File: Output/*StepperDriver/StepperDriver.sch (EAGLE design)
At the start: 12 parts

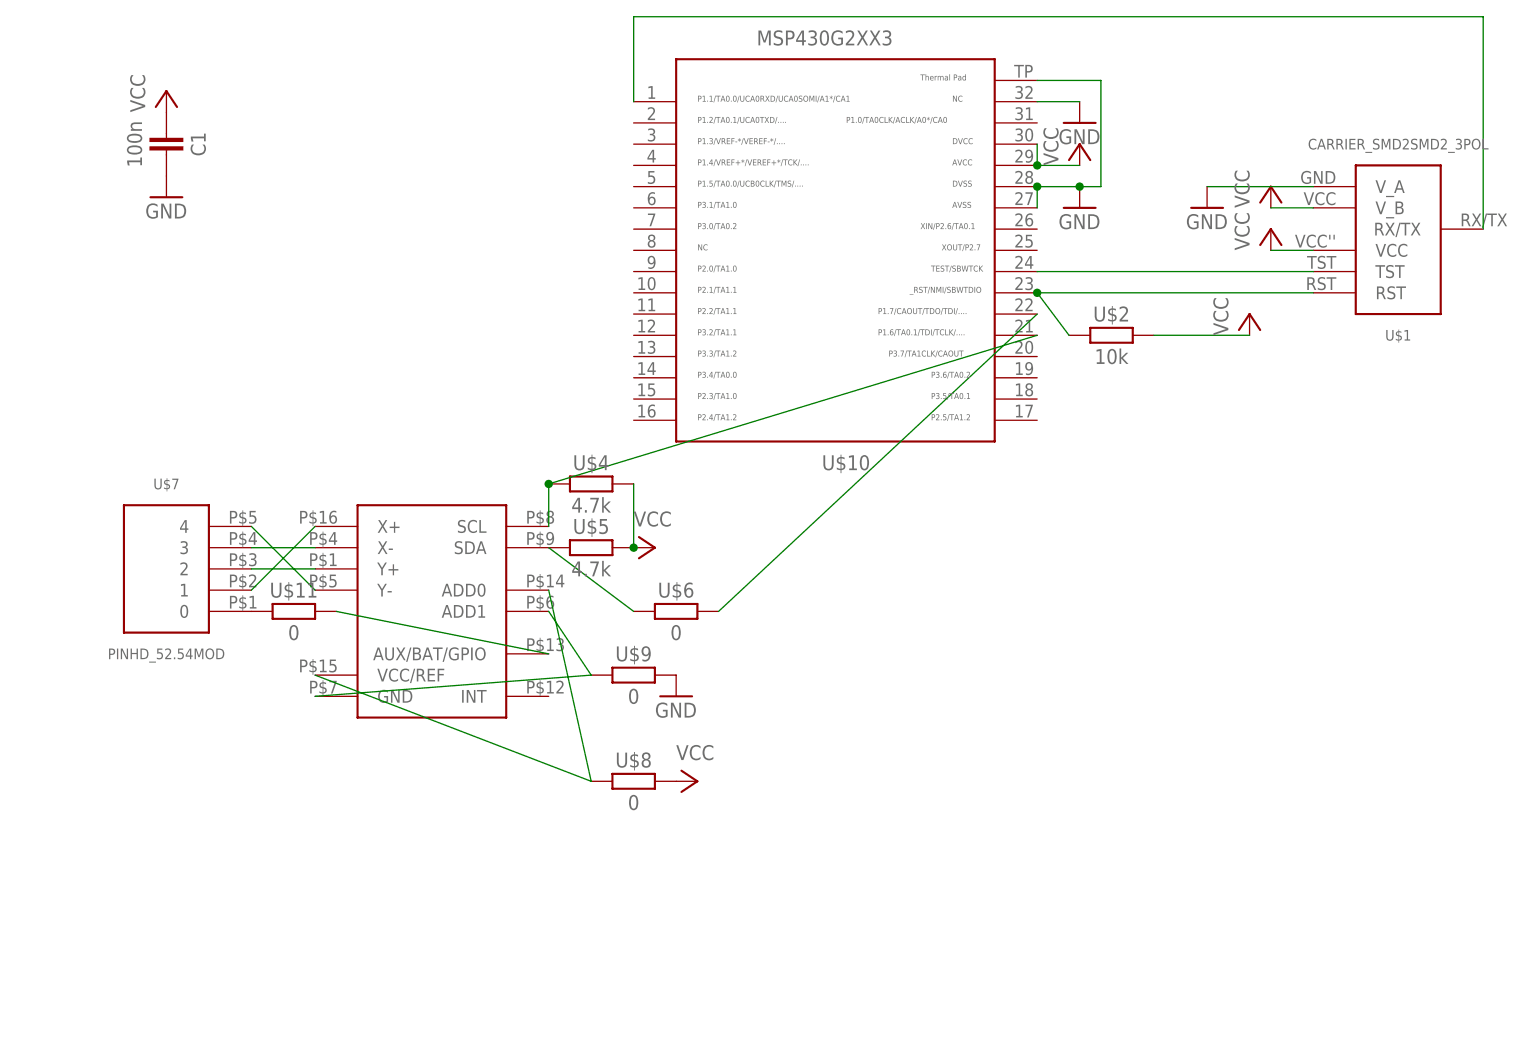
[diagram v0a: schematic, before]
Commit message: Update Pinheader
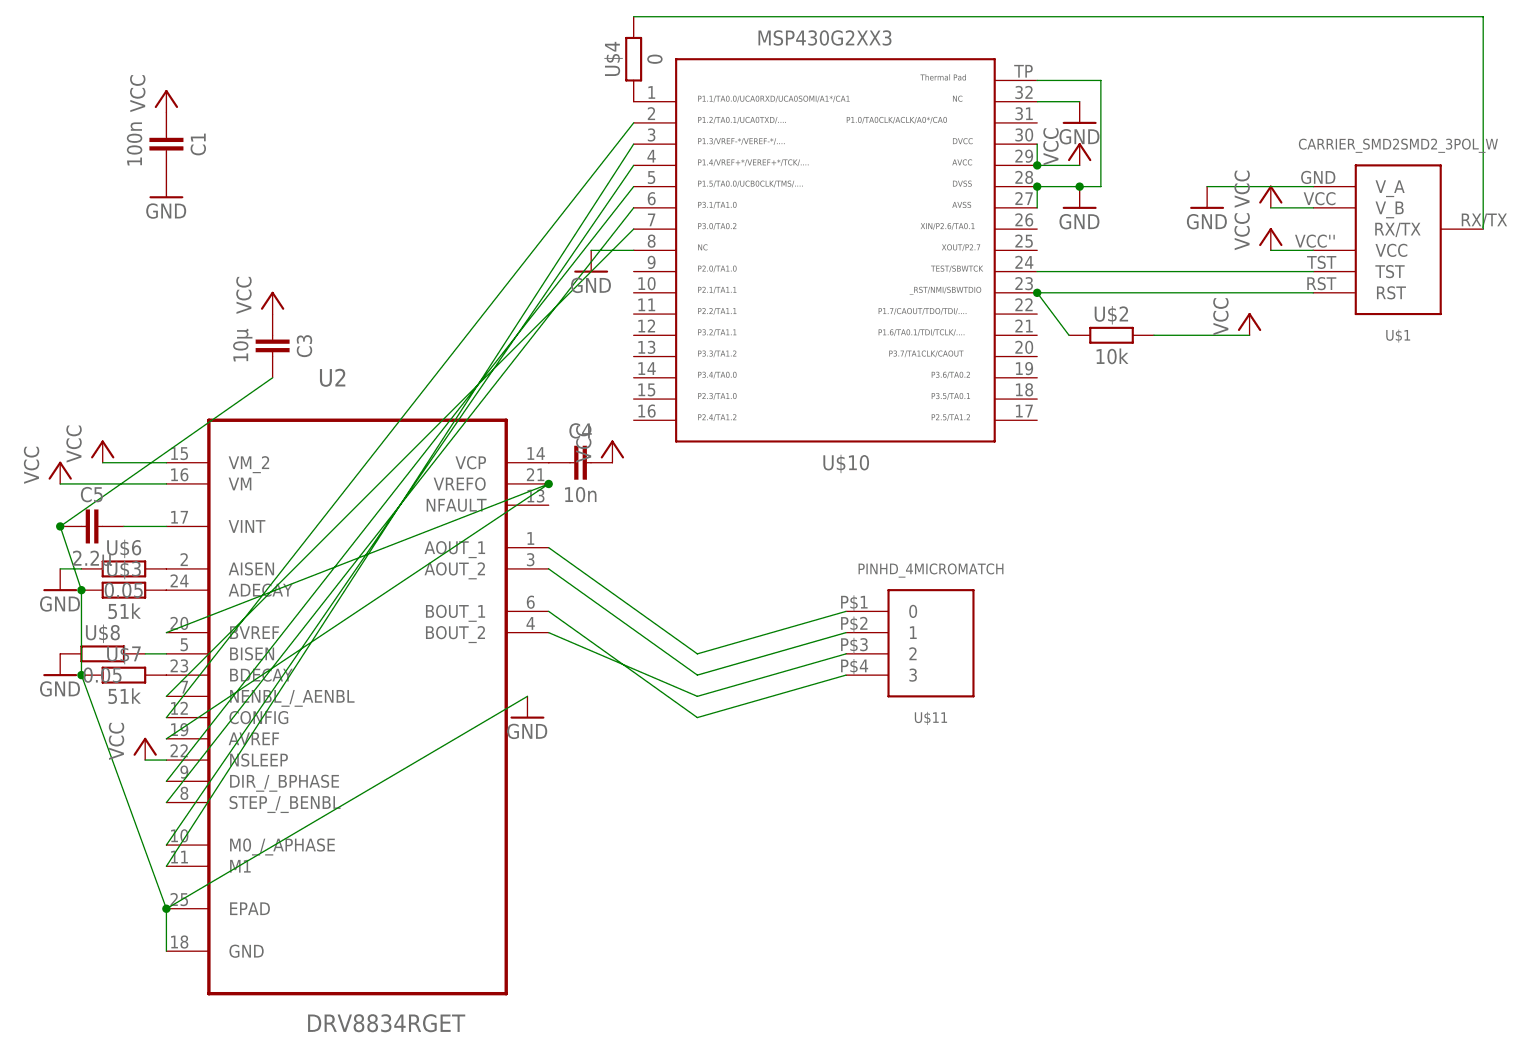
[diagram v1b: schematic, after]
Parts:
- removed U$5: 4.7k, thar:RESISTOR0603
- removed U$9: 0, thar:RESISTOR0603
- added C3: 10µ, thar:CAPACITOR
- added C4: 10n, thar:CAPACITOR
- added C5: 2.2µ, thar:CAPACITOR
- added U2: DRV8834RGET, DRV8834_QFN:DRV8834RGET
- U$1: value CARRIER_SMD2SMD2_3POL -> CARRIER_SMD2SMD2_3POL_W; device thar:CARRIER_SMD2SMD2_3POL -> thar:CARRIER_SMD2SMD2_3POL_W
- U$11: value 0 -> PINHD_4MICROMATCH; device thar:RESISTOR0603 -> thar:PINHD_4MICROMATCH
- U$3: value AD7879 -> 51k; device thar:AD7879 -> thar:RESISTOR0603
- U$4: value 4.7k -> 0
- U$6, U$8: value 0 -> 0.05
- U$7: value PINHD_52.54MOD -> 51k; device thar:PINHD_52.54MOD -> thar:RESISTOR0603
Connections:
- removed net N$15: U$10.22, U$6.2
- removed net N$17: U$3.ADD1, U$3.GND, U$9.1
- new net N$23: U$11.0, U2.AOUT_1
- new net N$24: U$11.1, U2.AOUT_2
- new net N$27: U2.AVREF, U2.BVREF, U2.VREFO
- new net N$29: U$10.4, U2.M0_/_APHASE
- new net N$32: U$10.3, U2.M1
- new net N$34: U$10.7, U2.NENBL_/_AENBL
- new net N$35: U$10.6, U2.STEP_/_BENBL
- new net N$36: U$10.2, U2.CONFIG
- new net N$37: U$10.5, U2.DIR_/_BPHASE
- net GND: now also C3.2, C5.1, U$10.8, U$3.1, U$6.1, U$7.1, U$8.1, U2.EPAD, U2.GND; no longer U$9.2
- net N$11: now also U$10.1, U$4.1; no longer U$3.Y+, U$7.2
- net N$12: now also U$4.2; no longer U$10.1
- net N$13: now also U$6.2, U2.AISEN; no longer U$3.X-, U$7.3
- net N$14: now also U$8.2, U2.BISEN; no longer U$3.Y-, U$7.4
- net N$16: now also U$11.3, U2.BOUT_1; no longer U$3.ADD0, U$3.VCC/REF, U$8.1
- net N$18: now also U2.BOUT_2; no longer U$3.AUX/BAT/GPIO
- net N$2: now also C5.2, U2.VINT; no longer U$10.21, U$3.SCL, U$4.1
- net N$5: now also C4.1, U2.VCP; no longer U$3.SDA, U$5.1, U$6.1
- net N$6: now also U$3.2, U2.ADECAY; no longer U$11.1, U$7.0
- net N$7: now also U$7.2, U2.BDECAY; no longer U$3.X+, U$7.1
- net VCC: now also C3.1, C4.2, U2.NSLEEP, U2.VM, U2.VM_2; no longer U$4.2, U$5.2, U$8.2
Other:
- moved on the sheet: U$4, U$6, U$8
